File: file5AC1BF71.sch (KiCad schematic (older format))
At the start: 16 parts

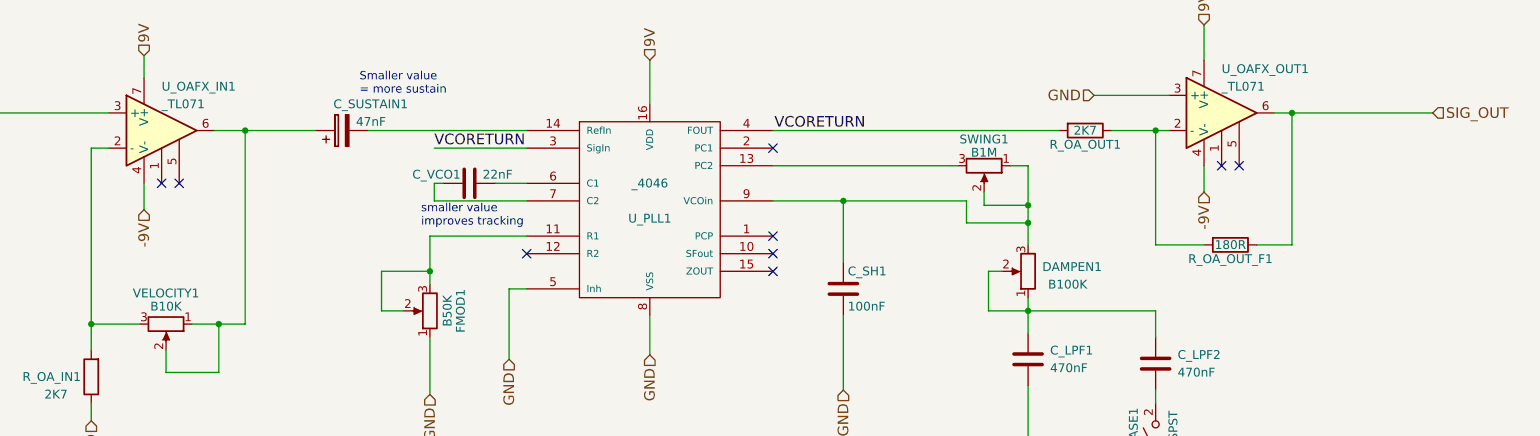
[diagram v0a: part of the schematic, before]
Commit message: UPDATE
ADDED FX OUPUT GAIN STAGE
ADDED FX/CLEAN MIXER OPAMP (WITH SINGLE BLEND POT CONTROL)
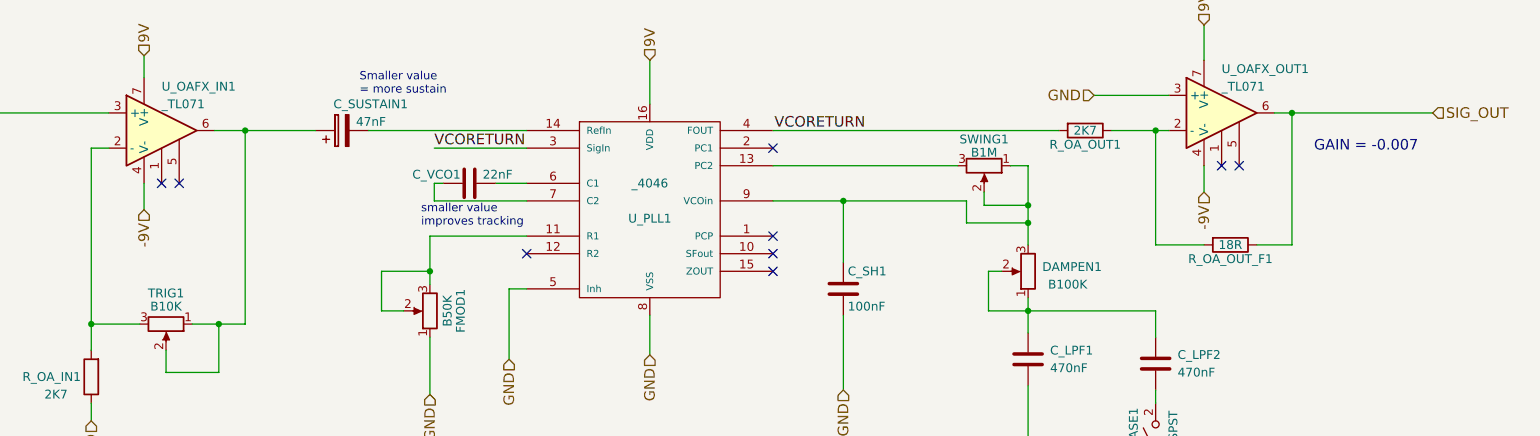
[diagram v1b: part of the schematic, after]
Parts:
- R_OA_OUT_F1: value 180R -> 18R
- renumbered VELOCITY1 to TRIG1
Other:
- note added: "GAIN = -0.007"
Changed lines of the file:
@@
 	-1   0    0    1
 $EndComp
-Wire Wire Line
-	2350 3275 2350 4425
-Wire Wire Line
-	2350 3275 2450 3275
-Wire Wire Line
-	2350 4275 2625 4275
-Connection ~ 2350 4275
-Wire Wire Line
-	2925 4275 3225 4275
-Wire Wire Line
-	3225 4275 3225 3175
-Wire Wire Line
-	3050 3175 3625 3175
-Wire Wire Line
-	2350 4725 2350 4825
-Wire Wire Line
-	2650 2875 2650 2750
-Wire Wire Line
-	2650 3475 2650 3625
 $Comp
 L CP C_SUSTAIN1
@@
 	0    -1   -1   0
 $EndComp
-Connection ~ 3225 3175
 $Comp
 L C C_VCO1
@@
 	0    1    1    0
 $EndComp
-Wire Wire Line
-	4650 3475 4825 3475
-Wire Wire Line
-	4350 3475 4300 3475
-Wire Wire Line
-	4300 3475 4300 3575
-Wire Wire Line
-	4300 3575 4825 3575
-Wire Wire Line
-	4000 3975 4275 3975
-Wire Wire Line
-	4825 4075 4725 4075
-Wire Wire Line
-	4725 4075 4725 4475
-Wire Wire Line
-	4825 3275 4300 3275
 Text Label 6750 3175 2    60   ~ 0
 VCORETURN
@@
 NoConn ~ 6225 3775
 NoConn ~ 6225 3275
-Wire Wire Line
-	5525 4225 5525 4450
-Wire Wire Line
-	5525 3025 5525 2775
 NoConn ~ 6225 3875
 NoConn ~ 4825 3875
-Wire Wire Line
-	3925 3175 4825 3175
-Wire Wire Line
-	6225 3375 7275 3375
-Wire Wire Line
-	7675 3375 7675 3825
 $Comp
 L C C_LPF1
@@
 	1    0    0    -1
 $EndComp
-Connection ~ 7675 3700
-Wire Wire Line
-	7675 3375 7575 3375
-Wire Wire Line
-	7675 4125 7675 4325
-Wire Wire Line
-	7675 4625 7675 5300
 NoConn ~ 2750 3475
 NoConn ~ 2850 3475
@@
 	1    0    0    -1
 $EndComp
-Wire Wire Line
-	4275 4675 4275 4350
-Wire Wire Line
-	4275 3775 4275 4050
 $Comp
 L NPOT SWING1
@@
 	0    1    1    0
 $EndComp
-Connection ~ 7675 3600
 $Comp
 L _4046 U_PLL1
@@
 	1    0    0    -1
 $EndComp
-Wire Wire Line
-	6225 3575 7325 3575
-Wire Wire Line
-	7325 3575 7325 3700
-Wire Wire Line
-	7325 3700 7675 3700
-Wire Wire Line
-	7425 3525 7425 3600
-Wire Wire Line
-	7425 3600 7675 3600
 $Comp
 L NPOT DAMPEN1
@@
 	-1   0    0    1
 $EndComp
-Wire Wire Line
-	7450 4200 8400 4200
-Wire Wire Line
-	7450 4200 7450 3975
-Wire Wire Line
-	7450 3975 7525 3975
-Connection ~ 7675 4200
 $Comp
 L C C_SH1
@@
 	1    0    0    -1
 $EndComp
-Wire Wire Line
-	6625 3925 6625 3575
-Connection ~ 6625 3575
-Wire Wire Line
-	6625 4225 6625 4650
 $Comp
 L _TL071 U_OAFX_OUT1
@@
 	1    0    0    -1
 $EndComp
-Wire Wire Line
-	8675 2775 8675 2575
-Wire Wire Line
-	8675 3375 8675 3525
-Wire Wire Line
-	8400 3175 8400 3825
-Wire Wire Line
-	9175 3825 9175 3075
-Wire Wire Line
-	9075 3075 9975 3075
-Connection ~ 9175 3075
 NoConn ~ 8775 3375
 NoConn ~ 8875 3375
-Wire Wire Line
-	6225 3175 7850 3175
 Text Notes 3875 2975 0    47   ~ 0
 Smaller value \n= more sustain
@@
 smaller value \nimproves tracking
 $Comp
-L NPOT VELOCITY1
+L NPOT TRIG1
 U 1 1 5AC1C6EB
 P 2775 4275
-F 0 "VELOCITY1" V 2600 4275 50  0000 C CNN
+F 0 "TRIG1" V 2600 4275 50  0000 C CNN
 F 1 "B10K" V 2675 4275 50  0000 C CNN
 F 2 "" H 2775 4275 50  0001 C CNN
@@
 	0    1    1    0
 $EndComp
-Wire Wire Line
-	2775 4425 2775 4550
-Wire Wire Line
-	2775 4550 3075 4550
-Wire Wire Line
-	3075 4550 3075 4275
-Connection ~ 3075 4275
 $Comp
 L NPOT FMOD1
@@
 	-1   0    0    1
 $EndComp
-Wire Wire Line
-	4125 4200 4000 4200
-Wire Wire Line
-	4000 4200 4000 3975
-Connection ~ 4275 3975
 $Comp
 L SW_SPST RELEASE1
@@
 	1    0    0    -1
 $EndComp
-Wire Wire Line
-	8400 4650 8400 4725
-Wire Wire Line
-	8400 4200 8400 4350
-Wire Wire Line
-	8400 5125 8400 5300
-Wire Wire Line
-	4825 3775 4275 3775
-Wire Wire Line
-	1775 3075 2450 3075
-Wire Wire Line
-	8475 2975 8050 2975
 $Comp
 L R R_OA_OUT1
@@
 	0    1    1    0
 $EndComp
-Wire Wire Line
-	8150 3175 8475 3175
-Connection ~ 8400 3175
-$Comp
-L R R_OA_OUT_F1
-U 1 1 5AC1C721
-P 8825 3825
-F 0 "R_OA_OUT_F1" V 8905 3825 50  0000 C CNN
-F 1 "180R" V 8825 3825 50  0000 C CNN
-F 2 "" V 8755 3825 50  0001 C CNN
-F 3 "" H 8825 3825 50  0001 C CNN
-	1    8825 3825
-	0    1    1    0
-$EndComp
-Wire Wire Line
-	8400 3825 8675 3825
-Wire Wire Line
-	8975 3825 9175 3825
 Text HLabel 1775 3075 0    60   Input ~ 0
 SIG_IN
@@
 Text HLabel 8050 2975 0    60   Input ~ 0
 GND
+Wire Wire Line
+	8975 3825 9175 3825
+Wire Wire Line
+	8400 3825 8675 3825
+Connection ~ 8400 3175
+Wire Wire Line
+	8150 3175 8475 3175
+Wire Wire Line
+	8475 2975 8050 2975
+Wire Wire Line
+	1775 3075 2450 3075
+Wire Wire Line
+	4825 3775 4275 3775
+Wire Wire Line
+	8400 5125 8400 5300
+Wire Wire Line
+	8400 4200 8400 4350
+Wire Wire Line
+	8400 4650 8400 4725
+Connection ~ 4275 3975
+Wire Wire Line
+	4000 4200 4000 3975
+Wire Wire Line
+	4125 4200 4000 4200
+Connection ~ 3075 4275
+Wire Wire Line
+	3075 4550 3075 4275
+Wire Wire Line
+	2775 4550 3075 4550
+Wire Wire Line
+	2775 4425 2775 4550
+Wire Wire Line
+	6225 3175 7850 3175
+Connection ~ 9175 3075
+Wire Wire Line
+	9075 3075 9975 3075
+Wire Wire Line
+	9175 3825 9175 3075
+Wire Wire Line
+	8400 3175 8400 3825
+Wire Wire Line
+	8675 3375 8675 3525
+Wire Wire Line
+	8675 2775 8675 2575
+Wire Wire Line
+	6625 4225 6625 4650
+Connection ~ 6625 3575
+Wire Wire Line
+	6625 3925 6625 3575
+Connection ~ 7675 4200
+Wire Wire Line
+	7450 3975 7525 3975
+Wire Wire Line
+	7450 4200 7450 3975
+Wire Wire Line
+	7450 4200 8400 4200
+Wire Wire Line
+	7425 3600 7675 3600
+Wire Wire Line
+	7425 3525 7425 3600
+Wire Wire Line
+	7325 3700 7675 3700
+Wire Wire Line
+	7325 3575 7325 3700
+Wire Wire Line
+	6225 3575 7325 3575
+Connection ~ 7675 3600
+Wire Wire Line
+	4275 3775 4275 4050
+Wire Wire Line
+	4275 4675 4275 4350
+Wire Wire Line
+	7675 4625 7675 5300
+Wire Wire Line
+	7675 4125 7675 4325
+Wire Wire Line
+	7675 3375 7575 3375
+Connection ~ 7675 3700
+Wire Wire Line
+	7675 3375 7675 3825
+Wire Wire Line
+	6225 3375 7275 3375
+Wire Wire Line
+	3925 3175 4825 3175
+Wire Wire Line
+	5525 3025 5525 2775
+Wire Wire Line
+	5525 4225 5525 4450
+Wire Wire Line
+	4825 3275 4300 3275
+Wire Wire Line
+	4725 4075 4725 4475
+Wire Wire Line
+	4825 4075 4725 4075
+Wire Wire Line
+	4000 3975 4275 3975
+Wire Wire Line
+	4300 3575 4825 3575
+Wire Wire Line
+	4300 3475 4300 3575
+Wire Wire Line
+	4350 3475 4300 3475
+Wire Wire Line
+	4650 3475 4825 3475
+Connection ~ 3225 3175
+Wire Wire Line
+	2650 3475 2650 3625
+Wire Wire Line
+	2650 2875 2650 2750
+Wire Wire Line
+	2350 4725 2350 4825
+Wire Wire Line
+	3050 3175 3625 3175
+Wire Wire Line
+	3225 4275 3225 3175
+Wire Wire Line
+	2925 4275 3225 4275
+Connection ~ 2350 4275
+Wire Wire Line
+	2350 4275 2625 4275
+Wire Wire Line
+	2350 3275 2450 3275
+Wire Wire Line
+	2350 3275 2350 4425
+$Comp
+L R R_OA_OUT_F1
+U 1 1 5AC1C721
+P 8825 3825
+F 0 "R_OA_OUT_F1" V 8905 3825 50  0000 C CNN
+F 1 "18R" V 8825 3825 50  0000 C CNN
+F 2 "" V 8755 3825 50  0001 C CNN
+F 3 "" H 8825 3825 50  0001 C CNN
+	1    8825 3825
+	0    1    1    0
+$EndComp
+Text Notes 9300 3300 0    60   ~ 0
+GAIN = -0.007
 $EndSCHEMATC

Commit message: UPDATE
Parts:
- R_OA_OUT_F1: value 18R -> 15R
- renumbered RELEASE1 to HOLD1
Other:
- note added: "GAIN = -0.006"
- note added: "GAIN = 1.0-4.7"
- note removed: "GAIN = -0.007"
- moved on the sheet: R_OA_IN1, TRIG1
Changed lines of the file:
@@
 L R R_OA_IN1
 U 1 1 5AC1C65B
-P 2350 4575
-F 0 "R_OA_IN1" H 2575 4575 50  0000 C CNN
-F 1 "2K7" H 2550 4675 50  0000 C CNN
-F 2 "" V 2280 4575 50  0001 C CNN
-F 3 "" H 2350 4575 50  0001 C CNN
-	1    2350 4575
+P 2350 4125
+F 0 "R_OA_IN1" H 2575 4125 50  0000 C CNN
+F 1 "2K7" H 2550 4225 50  0000 C CNN
+F 2 "" V 2280 4125 50  0001 C CNN
+F 3 "" H 2350 4125 50  0001 C CNN
+	1    2350 4125
 	-1   0    0    1
 $EndComp
@@
 L NPOT TRIG1
 U 1 1 5AC1C6EB
-P 2775 4275
-F 0 "TRIG1" V 2600 4275 50  0000 C CNN
-F 1 "B10K" V 2675 4275 50  0000 C CNN
-F 2 "" H 2775 4275 50  0001 C CNN
-F 3 "" H 2775 4275 50  0001 C CNN
-	1    2775 4275
+P 2975 3825
+F 0 "TRIG1" V 2800 3825 50  0000 C CNN
+F 1 "B10K" V 2875 3825 50  0000 C CNN
+F 2 "" H 2975 3825 50  0001 C CNN
+F 3 "" H 2975 3825 50  0001 C CNN
+	1    2975 3825
 	0    1    1    0
 $EndComp
@@
 $EndComp
 $Comp
-L SW_SPST RELEASE1
+L SW_SPST HOLD1
 U 1 1 5AC1C700
 P 8400 4925
-F 0 "RELEASE1" H 8400 5050 50  0000 C CNN
+F 0 "HOLD1" H 8400 5050 50  0000 C CNN
 F 1 "SW_SPST" H 8400 4825 50  0000 C CNN
 F 2 "" H 8400 4925 50  0001 C CNN
@@
 Text HLabel 2650 2750 1    60   Input ~ 0
 9V
-Text HLabel 2650 3625 3    60   Input ~ 0
+Text HLabel 2650 3525 3    60   Input ~ 0
 -9V
-Text HLabel 2350 4825 3    60   Input ~ 0
+Text HLabel 2350 4375 3    60   Input ~ 0
 GND
 Text HLabel 4275 4675 3    60   Input ~ 0
@@
 Connection ~ 8400 3175
 Wire Wire Line
-	8150 3175 8475 3175
+	8150 3175 8400 3175
+Wire Wire Line
+	8400 3175 8475 3175
 Wire Wire Line
 	8475 2975 8050 2975
@@
 Wire Wire Line
 	4125 4200 4000 4200
-Connection ~ 3075 4275
-Wire Wire Line
-	3075 4550 3075 4275
-Wire Wire Line
-	2775 4550 3075 4550
-Wire Wire Line
-	2775 4425 2775 4550
+Connection ~ 3275 3825
+Wire Wire Line
+	3275 4100 3275 3825
+Wire Wire Line
+	2975 4100 3275 4100
+Wire Wire Line
+	2975 3975 2975 4100
 Wire Wire Line
 	6225 3175 7850 3175
 Connection ~ 9175 3075
 Wire Wire Line
-	9075 3075 9975 3075
+	9075 3075 9175 3075
+Wire Wire Line
+	9175 3075 9975 3075
 Wire Wire Line
 	9175 3825 9175 3075
@@
 	7450 4200 7450 3975
 Wire Wire Line
-	7450 4200 8400 4200
+	7450 4200 7675 4200
+Wire Wire Line
+	7675 4200 8400 4200
 Wire Wire Line
 	7425 3600 7675 3600
@@
 	7325 3575 7325 3700
 Wire Wire Line
-	6225 3575 7325 3575
+	6225 3575 6625 3575
+Wire Wire Line
+	6625 3575 7325 3575
 Connection ~ 7675 3600
 Wire Wire Line
-	4275 3775 4275 4050
+	4275 3775 4275 3975
+Wire Wire Line
+	4275 3975 4275 4050
 Wire Wire Line
 	4275 4675 4275 4350
@@
 	7675 4625 7675 5300
 Wire Wire Line
-	7675 4125 7675 4325
+	7675 4125 7675 4200
+Wire Wire Line
+	7675 4200 7675 4325
 Wire Wire Line
 	7675 3375 7575 3375
 Connection ~ 7675 3700
 Wire Wire Line
-	7675 3375 7675 3825
+	7675 3375 7675 3600
+Wire Wire Line
+	7675 3600 7675 3700
+Wire Wire Line
+	7675 3700 7675 3825
 Wire Wire Line
 	6225 3375 7275 3375
@@
 Wire Wire Line
 	4650 3475 4825 3475
-Connection ~ 3225 3175
-Wire Wire Line
-	2650 3475 2650 3625
+Connection ~ 3400 3175
+Wire Wire Line
+	2650 3475 2650 3525
 Wire Wire Line
 	2650 2875 2650 2750
 Wire Wire Line
-	2350 4725 2350 4825
-Wire Wire Line
-	3050 3175 3625 3175
-Wire Wire Line
-	3225 4275 3225 3175
-Wire Wire Line
-	2925 4275 3225 4275
-Connection ~ 2350 4275
-Wire Wire Line
-	2350 4275 2625 4275
+	2350 4275 2350 4375
+Wire Wire Line
+	3050 3175 3400 3175
+Wire Wire Line
+	3400 3175 3625 3175
+Wire Wire Line
+	3400 3825 3400 3175
+Wire Wire Line
+	3125 3825 3275 3825
+Wire Wire Line
+	3275 3825 3400 3825
+Connection ~ 2350 3825
+Wire Wire Line
+	2350 3825 2825 3825
 Wire Wire Line
 	2350 3275 2450 3275
 Wire Wire Line
-	2350 3275 2350 4425
+	2350 3275 2350 3825
+Wire Wire Line
+	2350 3825 2350 3975
 $Comp
 L R R_OA_OUT_F1
@@
 P 8825 3825
 F 0 "R_OA_OUT_F1" V 8905 3825 50  0000 C CNN
-F 1 "18R" V 8825 3825 50  0000 C CNN
+F 1 "15R" V 8825 3825 50  0000 C CNN
 F 2 "" V 8755 3825 50  0001 C CNN
 F 3 "" H 8825 3825 50  0001 C CNN
@@
 $EndComp
 Text Notes 9300 3300 0    60   ~ 0
-GAIN = -0.007
+GAIN = -0.006
+Text Notes 2550 4325 0    60   ~ 0
+GAIN = 1.0-4.7
 $EndSCHEMATC

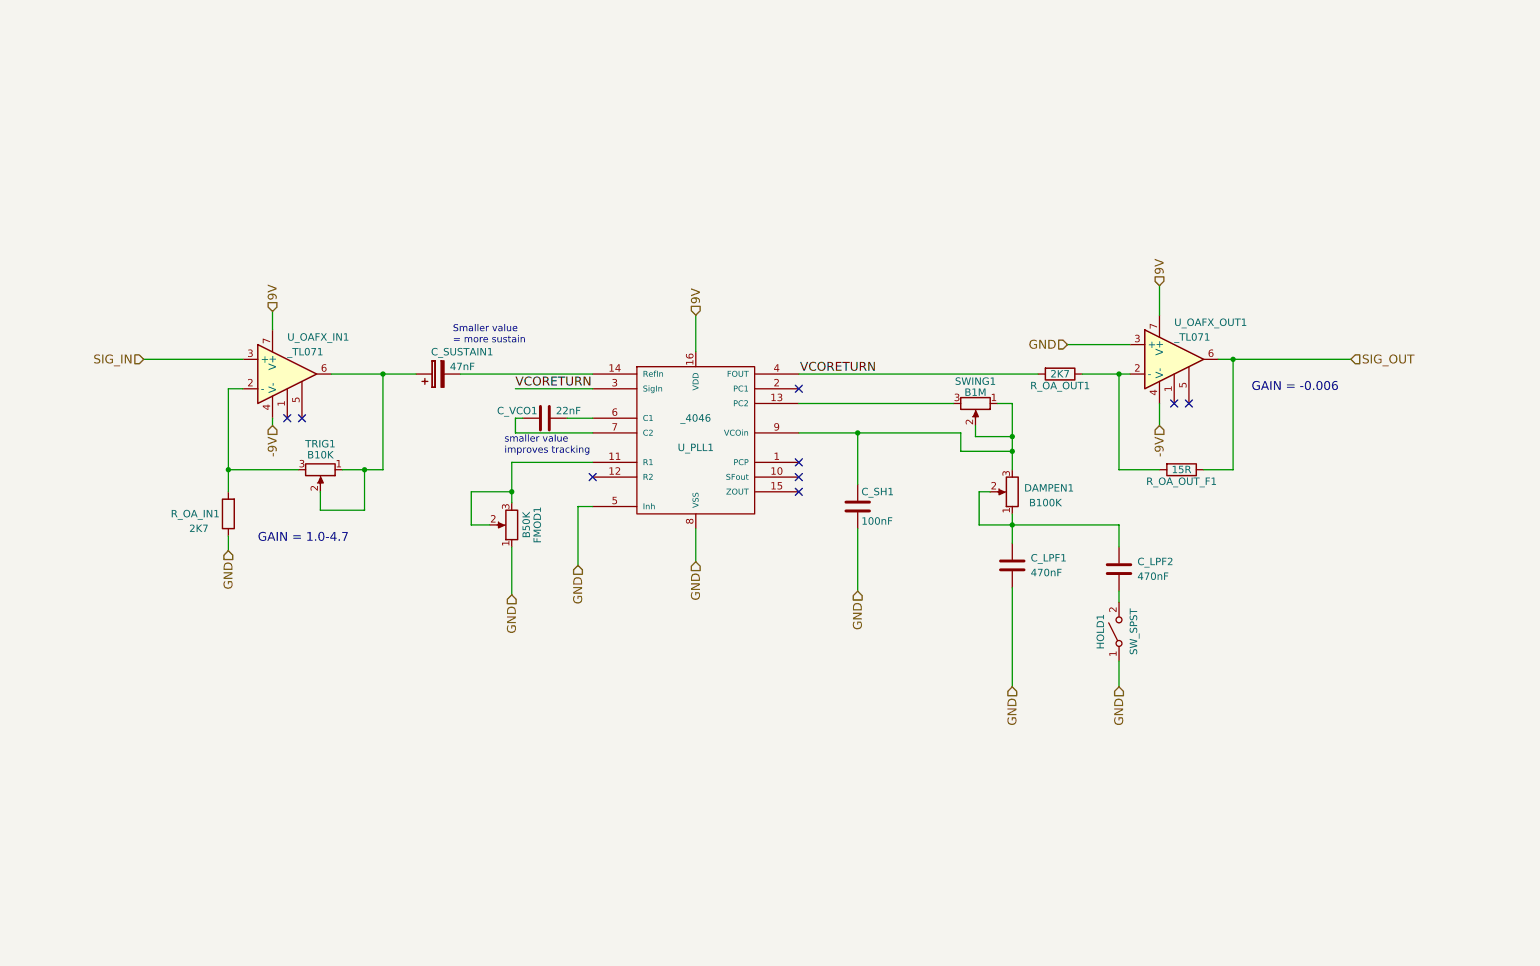
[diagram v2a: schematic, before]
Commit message: schematic design update
Added saw wave
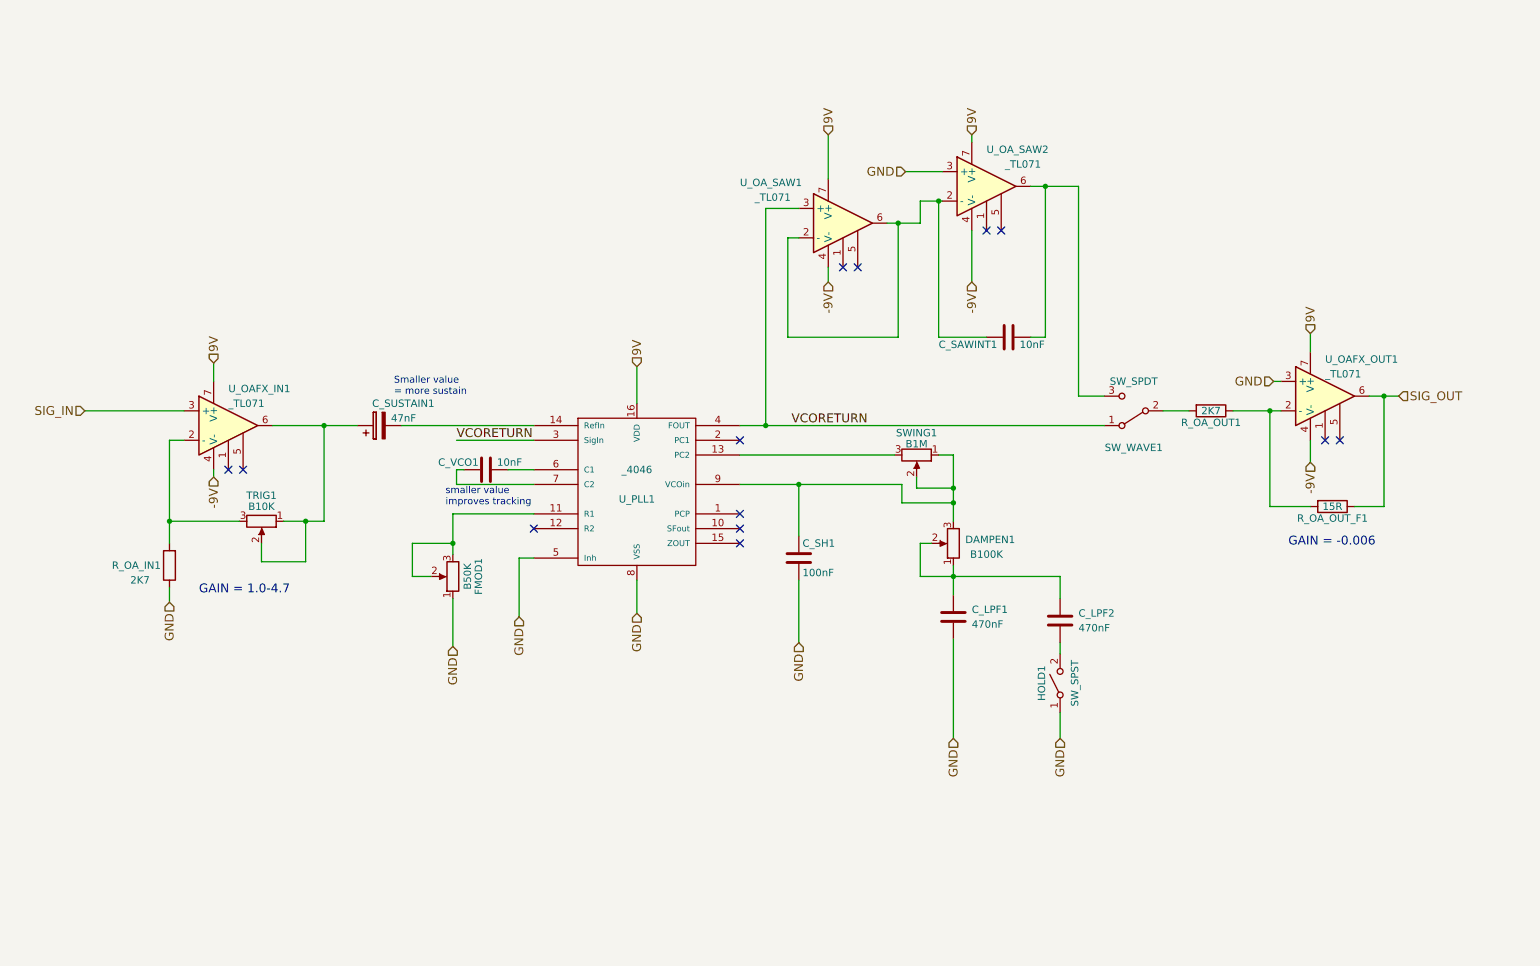
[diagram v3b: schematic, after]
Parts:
- added C_SAWINT1: 10nF, symbol C
- added SW_WAVE1: SW_SPDT, symbol SW_SPDT
- added U_OA_SAW1, U_OA_SAW2: _TL071, symbol _TL071
- C_VCO1: value 22nF -> 10nF
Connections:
- net -9V: now also U_OA_SAW1.4 (V-), U_OA_SAW2.4 (V-)
- net 9V: now also U_OA_SAW1.7 (V+), U_OA_SAW2.7 (V+)
- net GND: now also U_OA_SAW2.3 (+)
- net VCORETURN: now also SW_WAVE1.1 (A), U_OA_SAW1.3 (+); no longer R_OA_OUT1.2
- new net: C_SAWINT1.2, U_OA_SAW1.2 (-), U_OA_SAW1.6, U_OA_SAW2.2 (-)
- new net: C_SAWINT1.1, SW_WAVE1.3 (C), U_OA_SAW2.6
- new net: R_OA_OUT1.2, SW_WAVE1.2 (B)
- no-connect marks 9 -> 13
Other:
- moved on the sheet: C_LPF1, C_LPF2, C_SH1, C_SUSTAIN1, C_VCO1, DAMPEN1, FMOD1, HOLD1, R_OA_IN1, R_OA_OUT1, R_OA_OUT_F1, SWING1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
